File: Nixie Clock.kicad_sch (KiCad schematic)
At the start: 6 parts, among them J1 USB_C_Receptacle_USB2.0, U1 ESP32-S2-WROVER

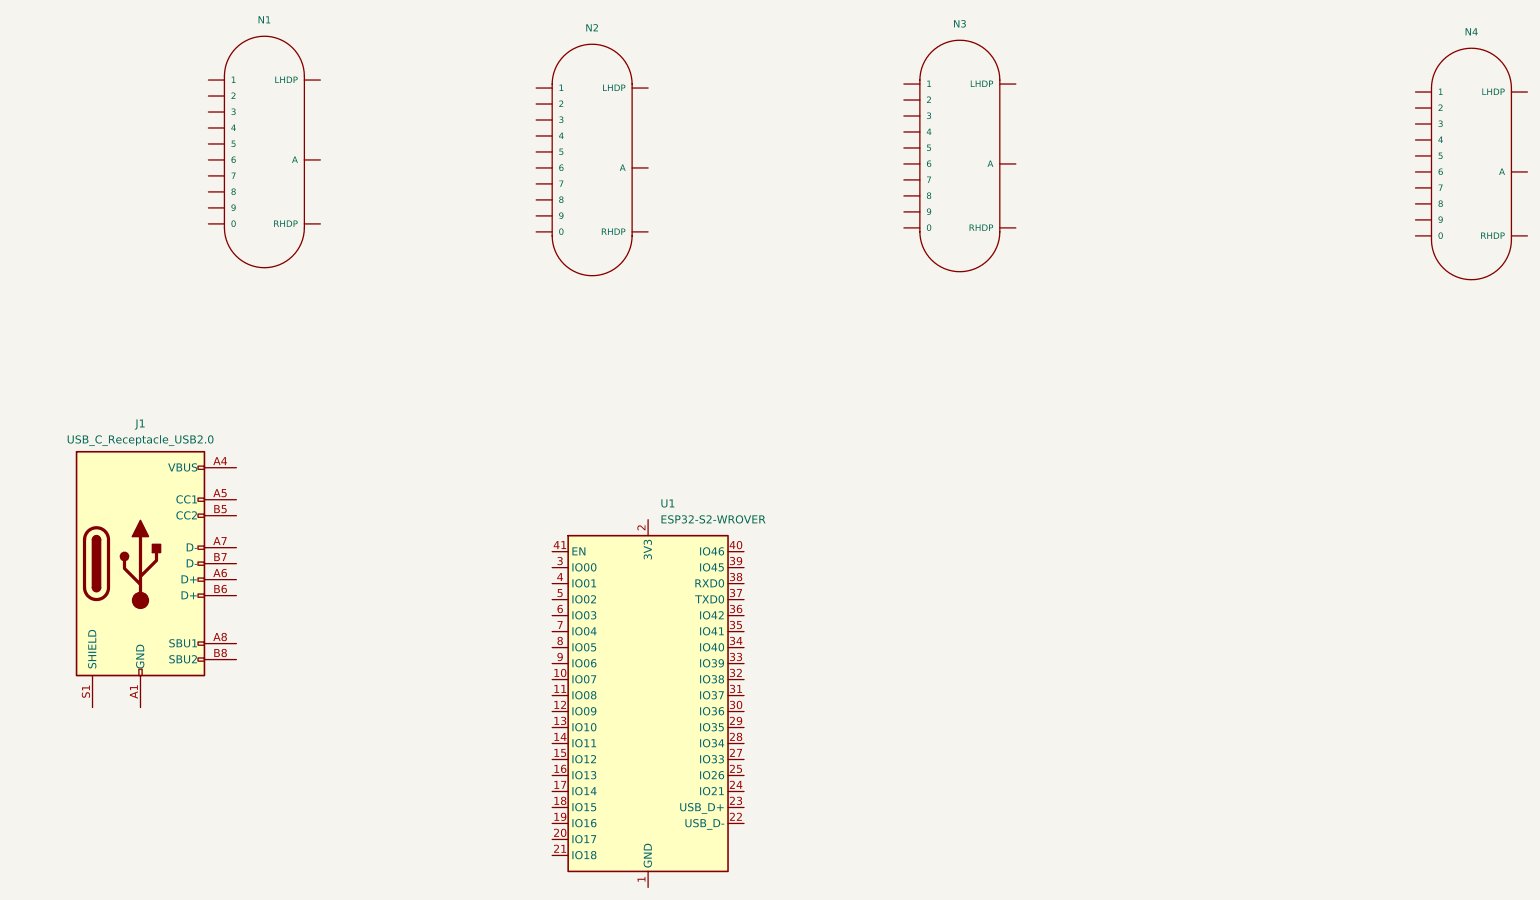
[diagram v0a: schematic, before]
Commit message: Created top plate ideas
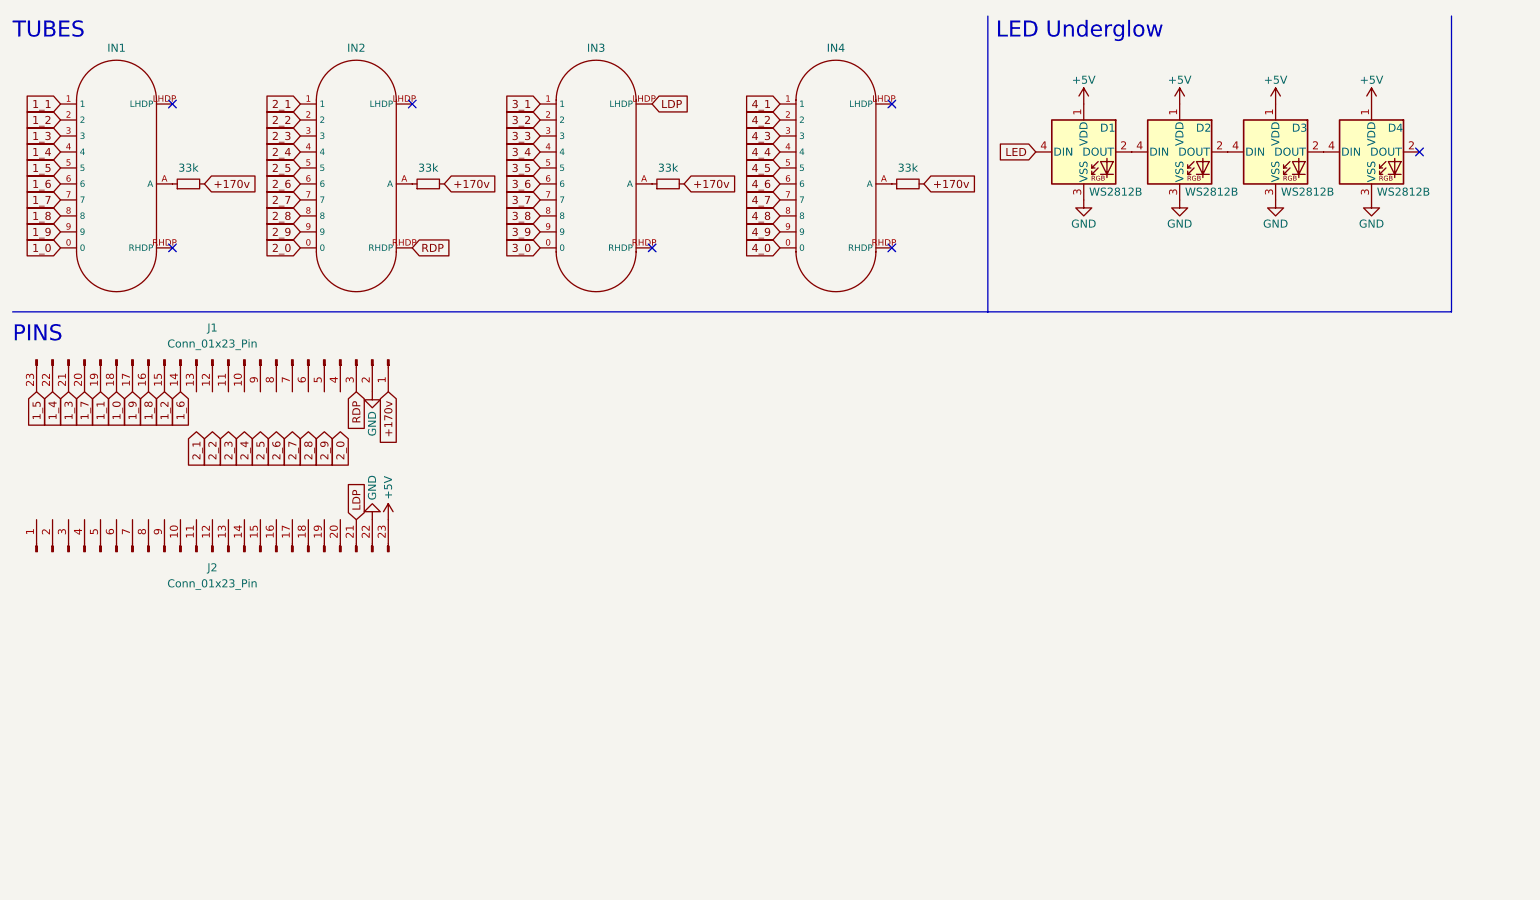
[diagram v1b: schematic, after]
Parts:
- removed J1: USB_C_Receptacle_USB2.0, Connector_USB:USB_C_Receptacle_HRO_TYPE-C-31-M-12, symbol Connector:USB_C_Receptacle_USB2.0
- removed N1, N2, N3, N4: IN-16, nixies-us:nixies-us-IN-16, symbol nixies-us:IN-16
- removed U1: ESP32-S2-WROVER, RF_Module:ESP32-S3-WROOM-1, symbol RF_Module:ESP32-S2-WROVER
- added D1, D2, D3, D4: WS2812B, LED_SMD:LED_WS2812B_PLCC4_5.0x5.0mm_P3.2mm, symbol LED:WS2812B
- added IN1, IN2, IN3, IN4: ~, Indicator-Tube:IN-16, symbol Indicator_Tube:IN-16
- added J1, J2: Conn_01x23_Pin, Connector_PinHeader_2.54mm:PinHeader_1x23_P2.54mm_Vertical_SMD_Pin1Left, symbol Connector:Conn_01x23_Pin
- added R1, R2, R3, R4: 33k, Resistor_SMD:R_0402_1005Metric_Pad0.72x0.64mm_HandSolder, symbol Device:R_Small
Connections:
- new net: IN2.A, R2.1
- new net: IN3.A, R3.1
- new net: D3.2 (DOUT), D4.4 (DIN)
- new net: D2.2 (DOUT), D3.4 (DIN)
- new net: D1.2 (DOUT), D2.4 (DIN)
- new net: IN4.A, R4.1
- new net: IN1.A, R1.1
- new net +170v: J1.1 (Pin_1), R1.2, R2.2, R3.2, R4.2
- new net +5V: D1.1 (VDD), D2.1 (VDD), D3.1 (VDD), D4.1 (VDD), J2.23 (Pin_23)
- new net 1_0: IN1.0, J1.18 (Pin_18)
- new net 1_1: IN1.1, J1.19 (Pin_19)
- new net 1_2: IN1.2, J1.15 (Pin_15)
- new net 1_3: IN1.3, J1.21 (Pin_21)
- new net 1_4: IN1.4, J1.22 (Pin_22)
- new net 1_5: IN1.5, J1.23 (Pin_23)
- new net 1_6: IN1.6, J1.14 (Pin_14)
- new net 1_7: IN1.7, J1.20 (Pin_20)
- new net 1_8: IN1.8, J1.16 (Pin_16)
- new net 1_9: IN1.9, J1.17 (Pin_17)
- new net 2_0: IN2.0
- new net 2_1: IN2.1
- new net 2_2: IN2.2
- new net 2_3: IN2.3
- new net 2_4: IN2.4
- new net 2_5: IN2.5
- new net 2_6: IN2.6
- new net 2_7: IN2.7
- new net 2_8: IN2.8
- new net 2_9: IN2.9
- new net 3_0: IN3.0
- new net 3_1: IN3.1
- new net 3_2: IN3.2
- new net 3_3: IN3.3
- new net 3_4: IN3.4
- new net 3_5: IN3.5
- new net 3_6: IN3.6
- new net 3_7: IN3.7
- new net 3_8: IN3.8
- new net 3_9: IN3.9
- new net 4_0: IN4.0
- new net 4_1: IN4.1
- new net 4_2: IN4.2
- new net 4_3: IN4.3
- new net 4_4: IN4.4
- new net 4_5: IN4.5
- new net 4_6: IN4.6
- new net 4_7: IN4.7
- new net 4_8: IN4.8
- new net 4_9: IN4.9
- new net GND: D1.3 (VSS), D2.3 (VSS), D3.3 (VSS), D4.3 (VSS), J1.2 (Pin_2), J2.22 (Pin_22)
- new net LDP: IN3.LHDP, J2.21 (Pin_21)
- new net LED: D1.4 (DIN)
- new net RDP: IN2.RHDP, J1.3 (Pin_3)
- no-connect marks 0 -> 7
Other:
- note added: "LED Underglow"
- note added: "PINS"
- note added: "TUBES"

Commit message: Finished top plate
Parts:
- removed D1, D2, D3, D4: WS2812B, LED_SMD:LED_WS2812B_PLCC4_5.0x5.0mm_P3.2mm, symbol LED:WS2812B
- R1, R2, R3, R4: footprint Resistor_SMD:R_0402_1005Metric_Pad0.72x0.64mm_HandSolder -> Resistor_SMD:R_0805_2012Metric
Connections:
- net +5V is gone; now on net GND: J2.23 (Pin_23)
- net 2_0: now also J1.8 (Pin_8)
- net 2_1: now also J1.9 (Pin_9)
- net 2_2: now also J1.5 (Pin_5)
- net 2_3: now also J1.11 (Pin_11)
- net 2_4: now also J1.12 (Pin_12)
- net 2_5: now also J1.13 (Pin_13)
- net 2_6: now also J1.4 (Pin_4)
- net 2_7: now also J1.10 (Pin_10)
- net 2_8: now also J1.6 (Pin_6)
- net 2_9: now also J1.7 (Pin_7)
- net 3_0: now also J2.12 (Pin_12)
- net 3_1: now also J2.2 (Pin_2)
- net 3_2: now also J2.8 (Pin_8)
- net 3_3: now also J2.4 (Pin_4)
- net 3_4: now also J2.5 (Pin_5)
- net 3_5: now also J2.6 (Pin_6)
- net 3_6: now also J2.7 (Pin_7)
- net 3_7: now also J2.3 (Pin_3)
- net 3_8: now also J2.10 (Pin_10)
- net 3_9: now also J2.11 (Pin_11)
- net 4_0: now also J2.22 (Pin_22)
- net 4_1: now also J2.13 (Pin_13)
- net 4_2: now also J2.19 (Pin_19)
- net 4_3: now also J2.15 (Pin_15)
- net 4_4: now also J2.16 (Pin_16)
- net 4_5: now also J2.17 (Pin_17)
- net 4_6: now also J2.18 (Pin_18)
- net 4_7: now also J2.14 (Pin_14)
- net 4_8: now also J2.20 (Pin_20)
- net 4_9: now also J2.21 (Pin_21)
- net GND: now also J2.1 (Pin_1); no longer J2.22 (Pin_22)
- net LDP: now also J2.9 (Pin_9); no longer J2.21 (Pin_21)
- no-connect marks 7 -> 6
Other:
- note removed: "LED Underglow"
- moved on the sheet: J2
